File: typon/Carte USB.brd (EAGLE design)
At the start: 68.6 x 74.6 mm, 20 parts, among them T1 2N5088, T2 2N5088, T3 2N5088, T4 2N5088, X1 MKS1854-6-0-404, X2 PN61729-S, X4 87758-0216, X5 PN61729-S, X7 PN61729-S, X8 PN61729-S

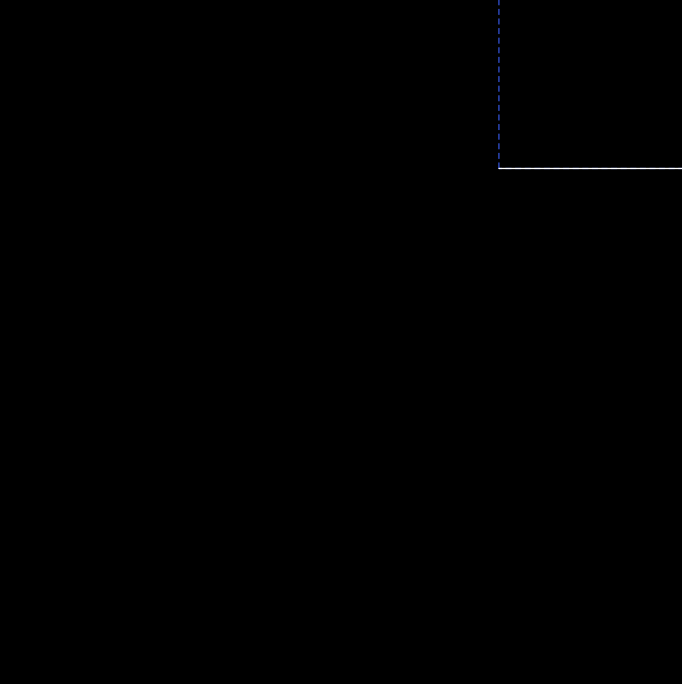
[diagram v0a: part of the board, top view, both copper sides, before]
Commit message: circuit colonne
simulation + typon  de la colonne
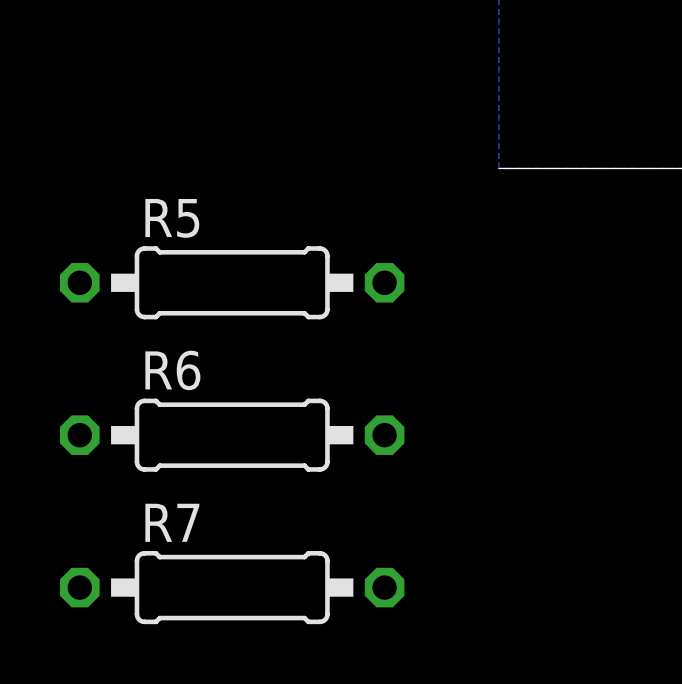
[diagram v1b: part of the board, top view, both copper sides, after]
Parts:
- added R5, R6, R7: (no value), rcl:0207/10
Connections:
- new net N$22: R5.2, R6.2, R7.2
- new net N$23: R5.1, R6.1, R7.1
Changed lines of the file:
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@@
 <element name="R3" library="rcl" package="0207/10" value="" x="118.11" y="69.85" rot="R180"/>
 <element name="R4" library="rcl" package="0207/10" value="" x="125.73" y="74.93" rot="R90"/>
+<element name="R5" library="rcl" package="0207/10" value="" x="82.55" y="12.7"/>
+<element name="R6" library="rcl" package="0207/10" value="" x="82.55" y="7.62"/>
+<element name="R7" library="rcl" package="0207/10" value="" x="82.55" y="2.54"/>
 </elements>
 <signals>
@@
 </polygon>
 </signal>
+<signal name="N$22">
+<contactref element="R5" pad="2"/>
+<contactref element="R6" pad="2"/>
+<contactref element="R7" pad="2"/>
+<contactref element="R7" pad="2"/>
+<wire x1="87.63" y1="7.62" x2="87.63" y2="12.7" width="0" layer="19" extent="1-1"/>
+<wire x1="87.63" y1="2.54" x2="87.63" y2="7.62" width="0" layer="19" extent="1-1"/>
+</signal>
+<signal name="N$23">
+<contactref element="R5" pad="1"/>
+<contactref element="R6" pad="1"/>
+<contactref element="R7" pad="1"/>
+<contactref element="R7" pad="1"/>
+<wire x1="77.47" y1="7.62" x2="77.47" y2="12.7" width="0" layer="19" extent="1-1"/>
+<wire x1="77.47" y1="2.54" x2="77.47" y2="7.62" width="0" layer="19" extent="1-1"/>
+</signal>
 </signals>
